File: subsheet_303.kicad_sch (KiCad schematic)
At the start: 4 parts, among them U303 8.010613 MHz, U304 74LS74_PHY

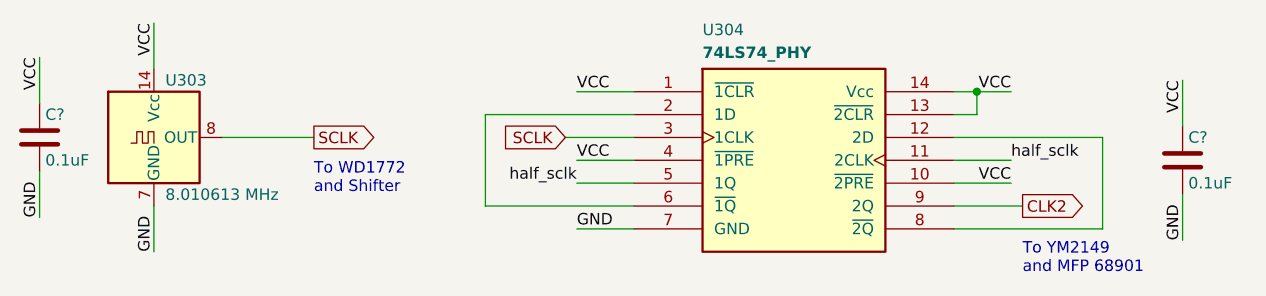
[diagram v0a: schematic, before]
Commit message: Resolves #3 : [schematic] annotate video port with signal name
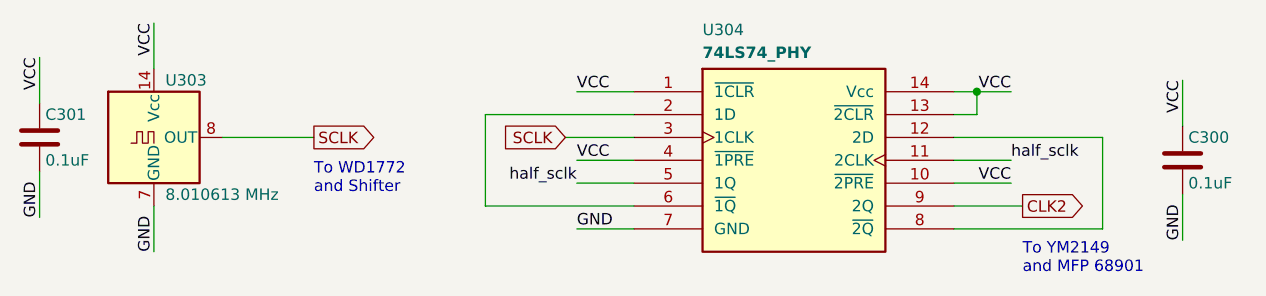
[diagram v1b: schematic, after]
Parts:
- gave numbers to parts that had none: 2
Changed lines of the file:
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@@
     (effects (font (size 1.27 1.27)) (justify left bottom))
   )
-  (label "VCC" (at 147.32 35.56 180)
+  (label "VCC" (at 147.32 35.56 180) (fields_autoplaced)
     (effects (font (size 1.27 1.27)) (justify right bottom))
   )
-  (label "VCC" (at 39.37 31.75 270)
+  (label "VCC" (at 39.37 31.75 270) (fields_autoplaced)
     (effects (font (size 1.27 1.27)) (justify right bottom))
   )
-  (label "VCC" (at 52.07 27.94 270)
+  (label "VCC" (at 52.07 27.94 270) (fields_autoplaced)
     (effects (font (size 1.27 1.27)) (justify right bottom))
   )
-  (label "VCC" (at 147.32 45.72 180)
+  (label "VCC" (at 147.32 45.72 180) (fields_autoplaced)
     (effects (font (size 1.27 1.27)) (justify right bottom))
   )
-  (label "VCC" (at 166.37 34.29 270)
+  (label "VCC" (at 166.37 34.29 270) (fields_autoplaced)
     (effects (font (size 1.27 1.27)) (justify right bottom))
   )
-  (label "GND" (at 52.07 53.34 90)
+  (label "GND" (at 52.07 53.34 90) (fields_autoplaced)
     (effects (font (size 1.27 1.27)) (justify left bottom))
   )
-  (label "GND" (at 99.06 50.8 0)
+  (label "GND" (at 99.06 50.8 0) (fields_autoplaced)
     (effects (font (size 1.27 1.27)) (justify left bottom))
   )
-  (label "half_sclk" (at 99.06 45.72 180)
+  (label "half_sclk" (at 99.06 45.72 180) (fields_autoplaced)
     (effects (font (size 1.27 1.27)) (justify right bottom))
   )
-  (label "half_sclk" (at 147.32 43.18 0)
+  (label "half_sclk" (at 147.32 43.18 0) (fields_autoplaced)
     (effects (font (size 1.27 1.27)) (justify left bottom))
   )
-  (label "VCC" (at 99.06 35.56 0)
+  (label "VCC" (at 99.06 35.56 0) (fields_autoplaced)
     (effects (font (size 1.27 1.27)) (justify left bottom))
   )
-  (label "GND" (at 39.37 49.53 90)
+  (label "GND" (at 39.37 49.53 90) (fields_autoplaced)
     (effects (font (size 1.27 1.27)) (justify left bottom))
   )
-  (label "VCC" (at 99.06 43.18 0)
+  (label "VCC" (at 99.06 43.18 0) (fields_autoplaced)
     (effects (font (size 1.27 1.27)) (justify left bottom))
   )
-  (label "GND" (at 166.37 52.07 90)
+  (label "GND" (at 166.37 52.07 90) (fields_autoplaced)
     (effects (font (size 1.27 1.27)) (justify left bottom))
   )
@@
   (symbol (lib_id "Device:C") (at 166.37 43.18 0) (unit 1)
     (in_bom yes) (on_board yes) (dnp no)
-    (property "Reference" "C?" (at 167.005 40.64 0)
+    (property "Reference" "C300" (at 167.005 40.64 0)
       (effects (font (size 1.27 1.27)) (justify left))
     )
@@
     (instances
       (project "motherboard"
-        (path "/4cb1fb88-82c9-4c30-a4b3-85a871b04fd2/00000000-0000-0000-0000-0000608a2359"
-          (reference "C?") (unit 1)
-        )
-        (path "/4cb1fb88-82c9-4c30-a4b3-85a871b04fd2/00000000-0000-0000-0000-000060a73cde"
-          (reference "C?") (unit 1)
-        )
         (path "/4cb1fb88-82c9-4c30-a4b3-85a871b04fd2/00000000-0000-0000-0000-000060abb05e"
           (reference "C300") (unit 1)
-        )
-        (path "/4cb1fb88-82c9-4c30-a4b3-85a871b04fd2/00000000-0000-0000-0000-00006089d0ba"
-          (reference "C?") (unit 1)
-        )
-        (path "/4cb1fb88-82c9-4c30-a4b3-85a871b04fd2/00000000-0000-0000-0000-000060ad8617"
-          (reference "C?") (unit 1)
-        )
-        (path "/4cb1fb88-82c9-4c30-a4b3-85a871b04fd2/00000000-0000-0000-0000-000060a1445f"
-          (reference "C?") (unit 1)
         )
       )
@@
   (symbol (lib_id "Device:C") (at 39.37 40.64 0) (unit 1)
     (in_bom yes) (on_board yes) (dnp no)
-    (property "Reference" "C?" (at 40.005 38.1 0)
+    (property "Reference" "C301" (at 40.005 38.1 0)
       (effects (font (size 1.27 1.27)) (justify left))
     )
@@
     (instances
       (project "motherboard"
-        (path "/4cb1fb88-82c9-4c30-a4b3-85a871b04fd2/00000000-0000-0000-0000-0000608a2359"
-          (reference "C?") (unit 1)
-        )
-        (path "/4cb1fb88-82c9-4c30-a4b3-85a871b04fd2/00000000-0000-0000-0000-000060a73cde"
-          (reference "C?") (unit 1)
-        )
         (path "/4cb1fb88-82c9-4c30-a4b3-85a871b04fd2/00000000-0000-0000-0000-000060abb05e"
           (reference "C301") (unit 1)
-        )
-        (path "/4cb1fb88-82c9-4c30-a4b3-85a871b04fd2/00000000-0000-0000-0000-00006089d0ba"
-          (reference "C?") (unit 1)
-        )
-        (path "/4cb1fb88-82c9-4c30-a4b3-85a871b04fd2/00000000-0000-0000-0000-000060ad8617"
-          (reference "C?") (unit 1)
-        )
-        (path "/4cb1fb88-82c9-4c30-a4b3-85a871b04fd2/00000000-0000-0000-0000-000060a1445f"
-          (reference "C?") (unit 1)
         )
       )
@@
           (reference "U303") (unit 1)
         )
-        (path "/4cb1fb88-82c9-4c30-a4b3-85a871b04fd2/00000000-0000-0000-0000-00006089d0c4"
-          (reference "U?") (unit 1)
-        )
       )
